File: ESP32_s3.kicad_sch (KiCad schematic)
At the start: 71 parts, among them J11 backup, J13 Jetson Power Supply, J14 TXRX, J15 TXRX2, J3 Conn_01x02, J4 Servo motor, J5 PJ-040DH, J7 Conn_01x02, J8 Conn_01x02, J9 Conn_01x02, Q1 BSS138, SW1 SW_Push, SW2 SW_Push, U1 ESP32-S3-WROOM-1-N8R2, U2 LM1117T-ADJ, U3 L298N, U4 TPS61088RHLR, Y1 Crystal

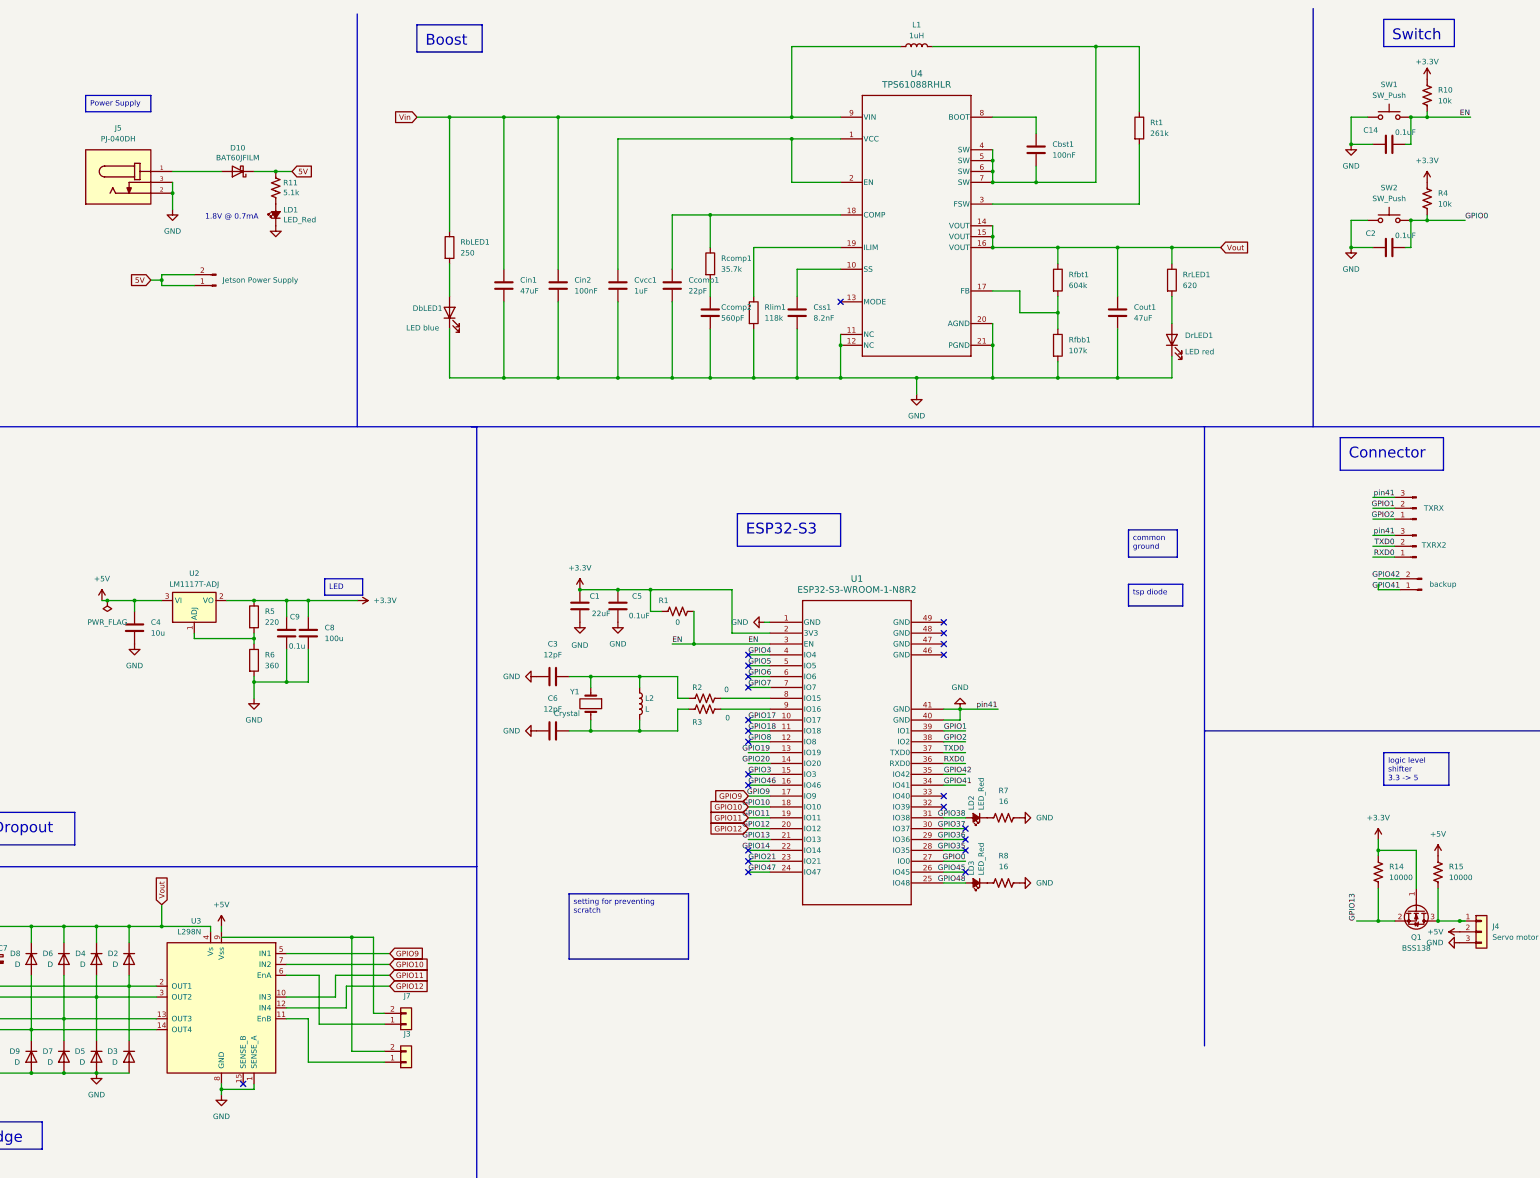
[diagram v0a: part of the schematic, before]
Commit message: update labels and traces
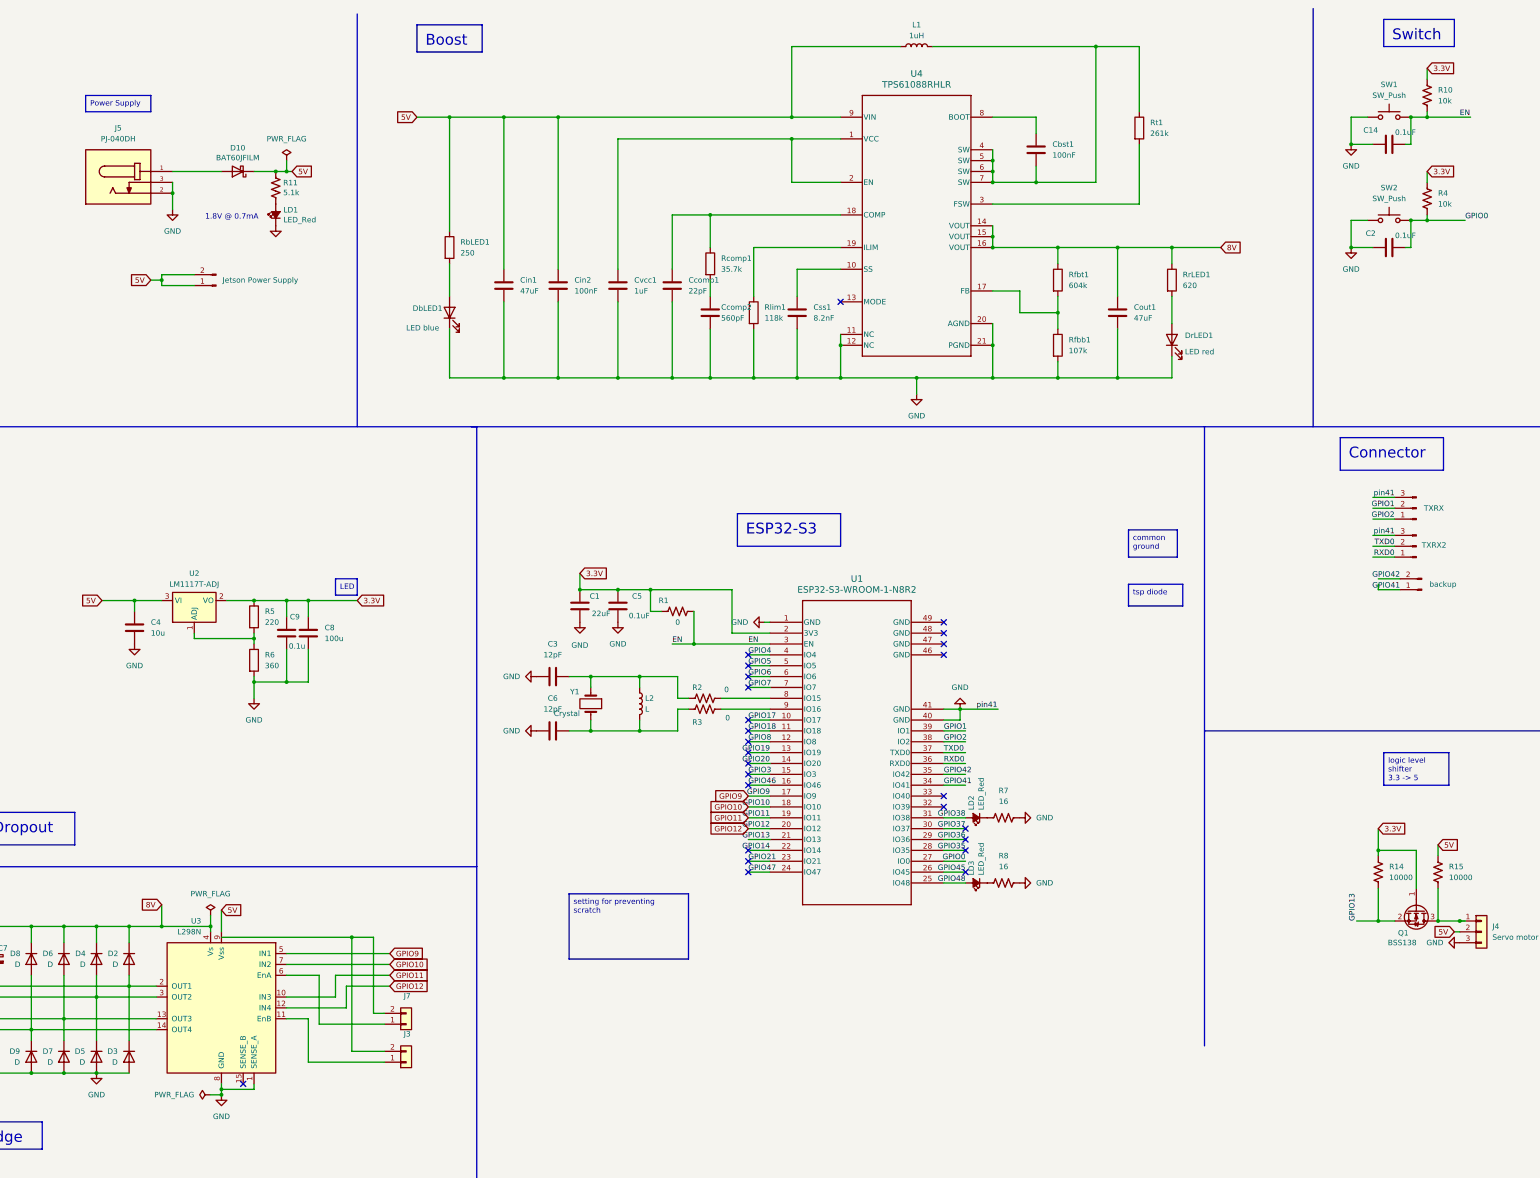
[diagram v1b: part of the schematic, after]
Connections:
- net +5V is gone; now on net 5V: C4.1, J4.2 (Pin_2), R15.2, U2.3 (VI), U3.9 (Vss)
- net Vin is gone; now on net 5V: Cin1.1, Cin2.1, L1.1, RbLED1.1, U4.9 (VIN)
- net +3.3V renamed 3.3V
- net Vout renamed 8V
- no-connect marks 24 -> 26

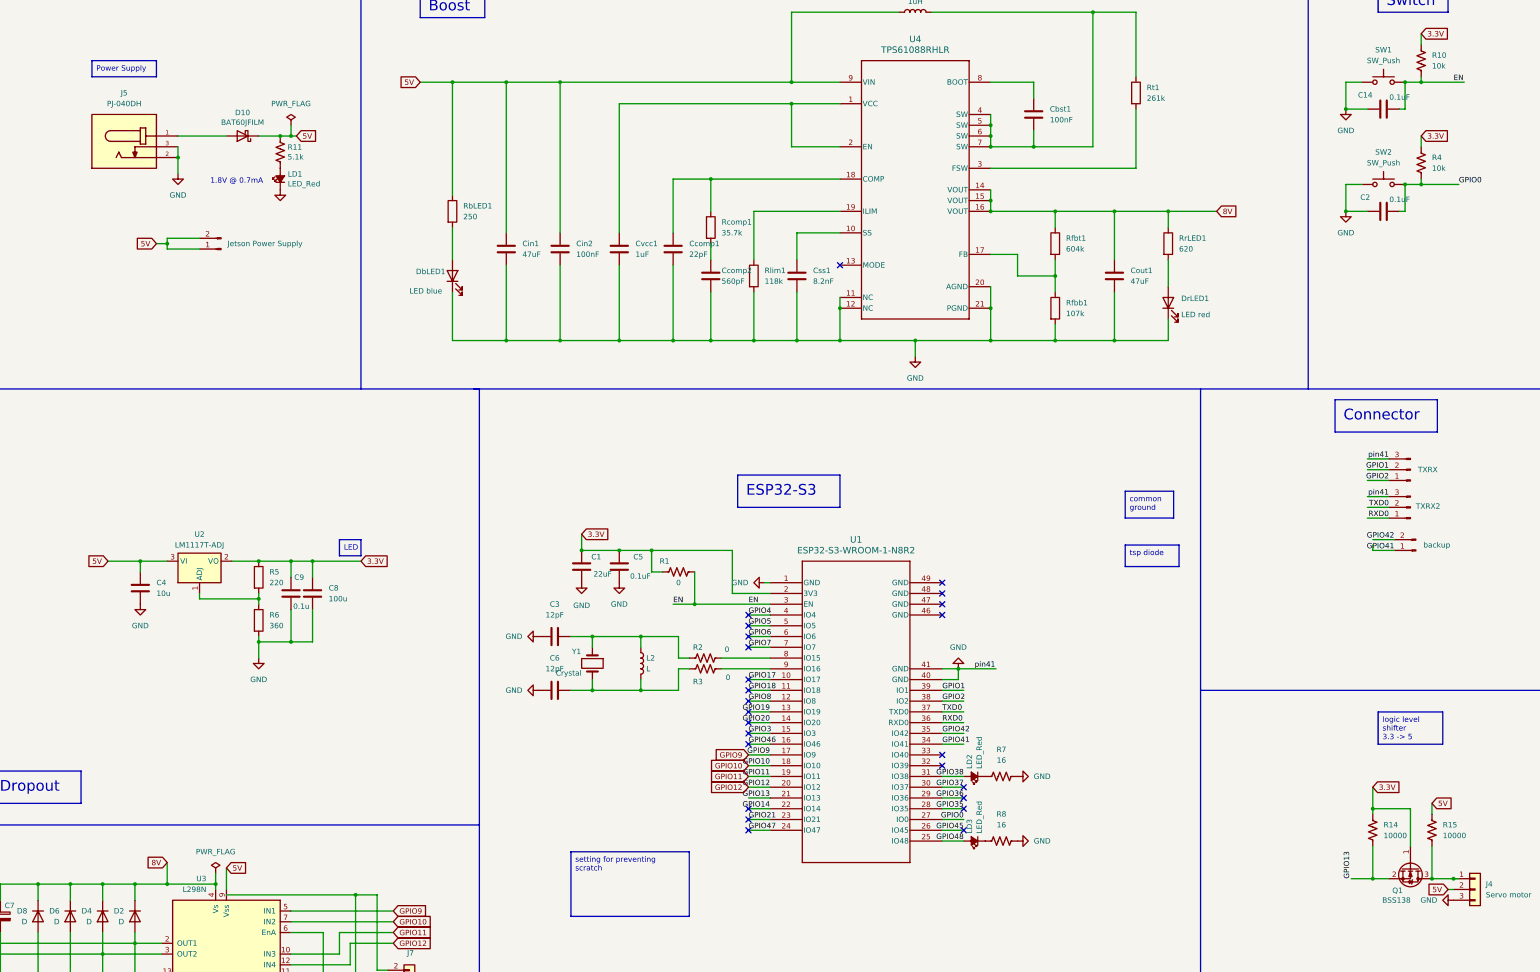
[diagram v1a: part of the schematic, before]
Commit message: fix net label
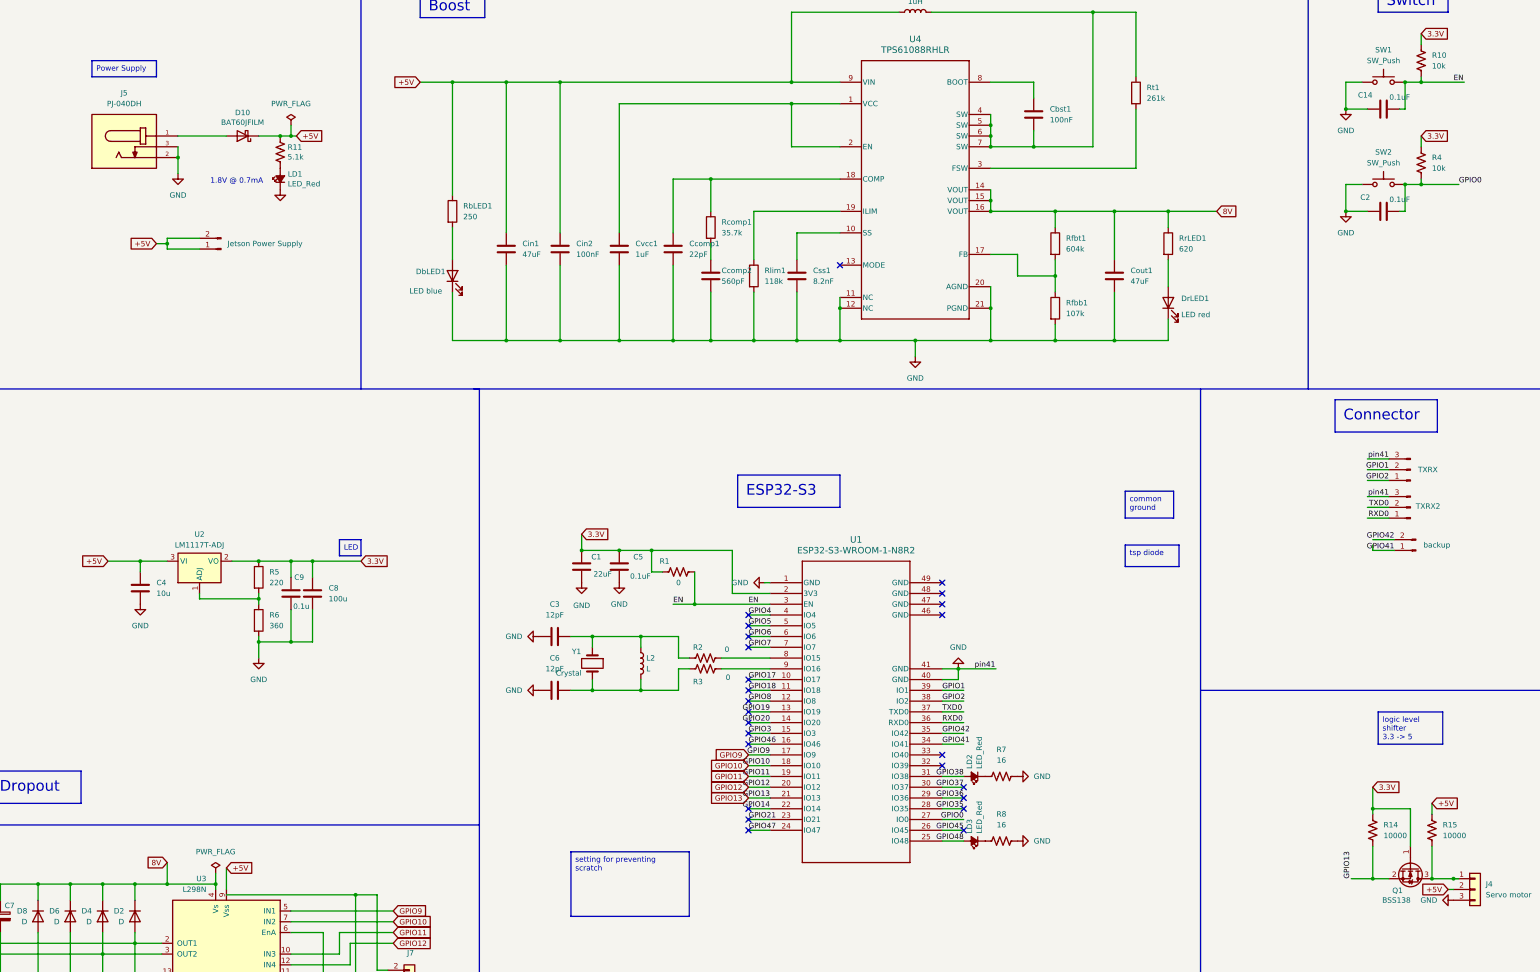
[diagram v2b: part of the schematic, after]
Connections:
- net 5V renamed +5V
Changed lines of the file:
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@@
 	)
 	(junction
-		(at 260.35 64.77)
+		(at 350.52 208.28)
 		(diameter 0)
 		(color 0 0 0 0)
 	)
 	(junction
-		(at 194.31 97.79)
+		(at 260.35 64.77)
 		(diameter 0)
 		(color 0 0 0 0)
 	)
 	(junction
-		(at 350.52 208.28)
+		(at 194.31 97.79)
 		(diameter 0)
 		(color 0 0 0 0)
@@
 	(wire
 		(pts
-			(xy 368.3 227.33) (xy 369.57 227.33)
-		)
-		(stroke
-			(width 0)
-			(type default)
-		)
-	)
-	(wire
-		(pts
 			(xy 248.92 193.04) (xy 254 193.04)
 		)
@@
 	(wire
 		(pts
+			(xy 368.3 227.33) (xy 369.57 227.33)
+		)
+		(stroke
+			(width 0)
+			(type default)
+		)
+	)
+	(wire
+		(pts
 			(xy 294.64 35.56) (xy 294.64 20.32)
 		)
@@
 	(wire
 		(pts
+			(xy 350.52 203.2) (xy 350.52 208.28)
+		)
+		(stroke
+			(width 0)
+			(type default)
+		)
+	)
+	(wire
+		(pts
 			(xy 26.67 226.06) (xy 26.67 229.87)
 		)
@@
 	(wire
 		(pts
-			(xy 350.52 203.2) (xy 350.52 208.28)
-		)
-		(stroke
-			(width 0)
-			(type default)
-		)
-	)
-	(wire
-		(pts
 			(xy 73.66 157.48) (xy 73.66 158.75)
 		)
@@
 	(wire
 		(pts
-			(xy 364.49 207.01) (xy 364.49 209.55)
-		)
-		(stroke
-			(width 0)
-			(type default)
-		)
-	)
-	(wire
-		(pts
 			(xy 347.98 60.96) (xy 344.17 60.96)
 		)
@@
 	(wire
 		(pts
+			(xy 364.49 207.01) (xy 364.49 209.55)
+		)
+		(stroke
+			(width 0)
+			(type default)
+		)
+	)
+	(wire
+		(pts
 			(xy 80.01 222.25) (xy 80.01 227.33)
 		)
@@
 		)
 	)
-	(global_label "5V"
+	(global_label "+5V"
 		(shape input)
 		(at 63.5 74.93 180)
@@
 		)
 		(property "Intersheetrefs" "${INTERSHEET_REFS}"
-			(at 58.2167 74.93 0)
+			(at 56.6443 74.93 0)
 			(effects
 				(font
@@
 		)
 	)
-	(global_label "5V"
+	(global_label "+5V"
 		(shape input)
 		(at 368.3 227.33 180)
@@
 		)
 		(property "Intersheetrefs" "${INTERSHEET_REFS}"
-			(at 363.0167 227.33 0)
+			(at 361.4443 227.33 0)
 			(effects
 				(font
@@
 		)
 	)
-	(global_label "5V"
+	(global_label "+5V"
 		(shape input)
 		(at 80.01 222.25 0)
@@
 		)
 		(property "Intersheetrefs" "${INTERSHEET_REFS}"
-			(at 85.2933 222.25 0)
+			(at 86.8657 222.25 0)
 			(effects
 				(font
@@
 		)
 	)
-	(global_label "5V"
+	(global_label "+5V"
 		(shape input)
 		(at 96.52 49.53 0)
@@
 		)
 		(property "Intersheetrefs" "${INTERSHEET_REFS}"
-			(at 101.8033 49.53 0)
+			(at 103.3757 49.53 0)
 			(effects
 				(font
@@
 		)
 	)
-	(global_label "5V"
+	(global_label "+5V"
 		(shape input)
 		(at 364.49 207.01 0)
@@
 		)
 		(property "Intersheetrefs" "${INTERSHEET_REFS}"
-			(at 369.7733 207.01 0)
+			(at 371.3457 207.01 0)
 			(effects
 				(font
@@
 		)
 	)
+	(global_label "GPIO13"
+		(shape input)
+		(at 203.2 205.74 180)
+		(fields_autoplaced yes)
+		(effects
+			(font
+				(size 1.27 1.27)
+			)
+			(justify right)
+		)
+		(property "Intersheetrefs" "${INTERSHEET_REFS}"
+			(at 193.3205 205.74 0)
+			(effects
+				(font
+					(size 1.27 1.27)
+				)
+				(justify right)
+				(hide yes)
+			)
+		)
+	)
 	(global_label "GPIO10"
 		(shape input)
@@
 		)
 	)
-	(global_label "5V"
+	(global_label "+5V"
 		(shape input)
 		(at 125.73 36.83 180)
@@
 		)
 		(property "Intersheetrefs" "${INTERSHEET_REFS}"
-			(at 120.4467 36.83 0)
+			(at 118.8743 36.83 0)
 			(effects
 				(font
@@
 		)
 	)
-	(global_label "5V"
+	(global_label "+5V"
 		(shape input)
 		(at 52.07 149.86 180)
@@
 		)
 		(property "Intersheetrefs" "${INTERSHEET_REFS}"
-			(at 46.7867 149.86 0)
+			(at 45.2143 149.86 0)
 			(effects
 				(font

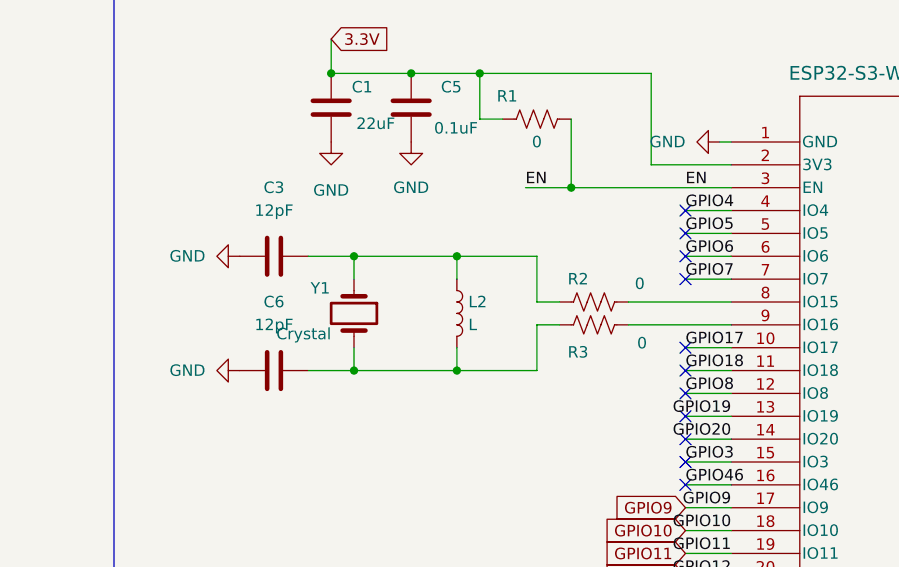
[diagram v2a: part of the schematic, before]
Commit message: delete 40MHZ crystal oscillator
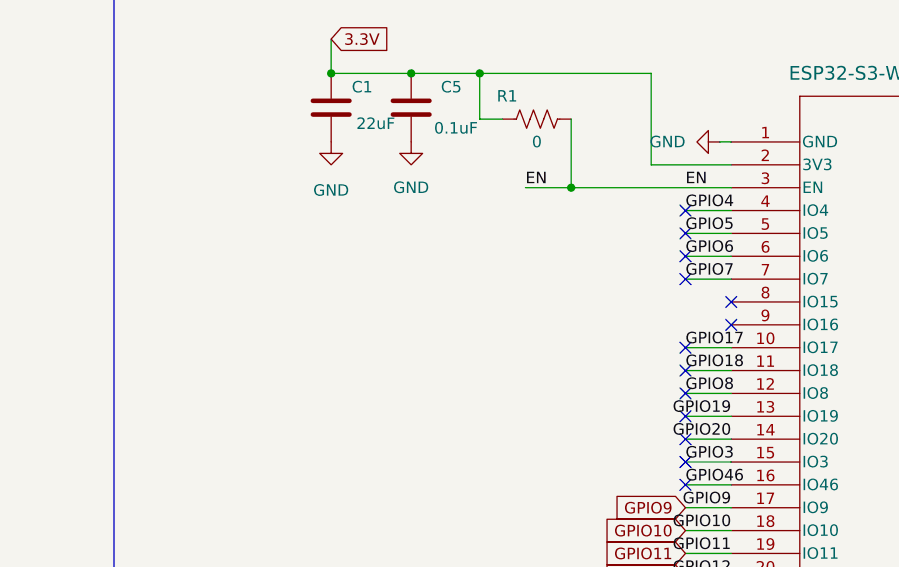
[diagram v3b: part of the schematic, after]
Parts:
- removed C3, C6: 12pF, CC1206JKNPODBN120:CAP_CC1206_YAG, symbol Device:C
- removed L2: L, LQW2BAN24NG00L:INDC2015X152N, symbol Device:L
- removed R2, R3: 0, RMCF1206ZR0R00:RESC3216X70N, symbol Device:R_US
- removed Y1: Crystal, crystal:XTAL_ABM12W-40.0000MHZ-6-B1U-T3, symbol Device:Crystal
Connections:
- no-connect marks 26 -> 28
